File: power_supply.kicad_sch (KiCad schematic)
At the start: 18 parts, among them J2 Conn_01x01_Male, J4 Conn_01x01_Male, U4 AP63203WU, U5 AP63205WU

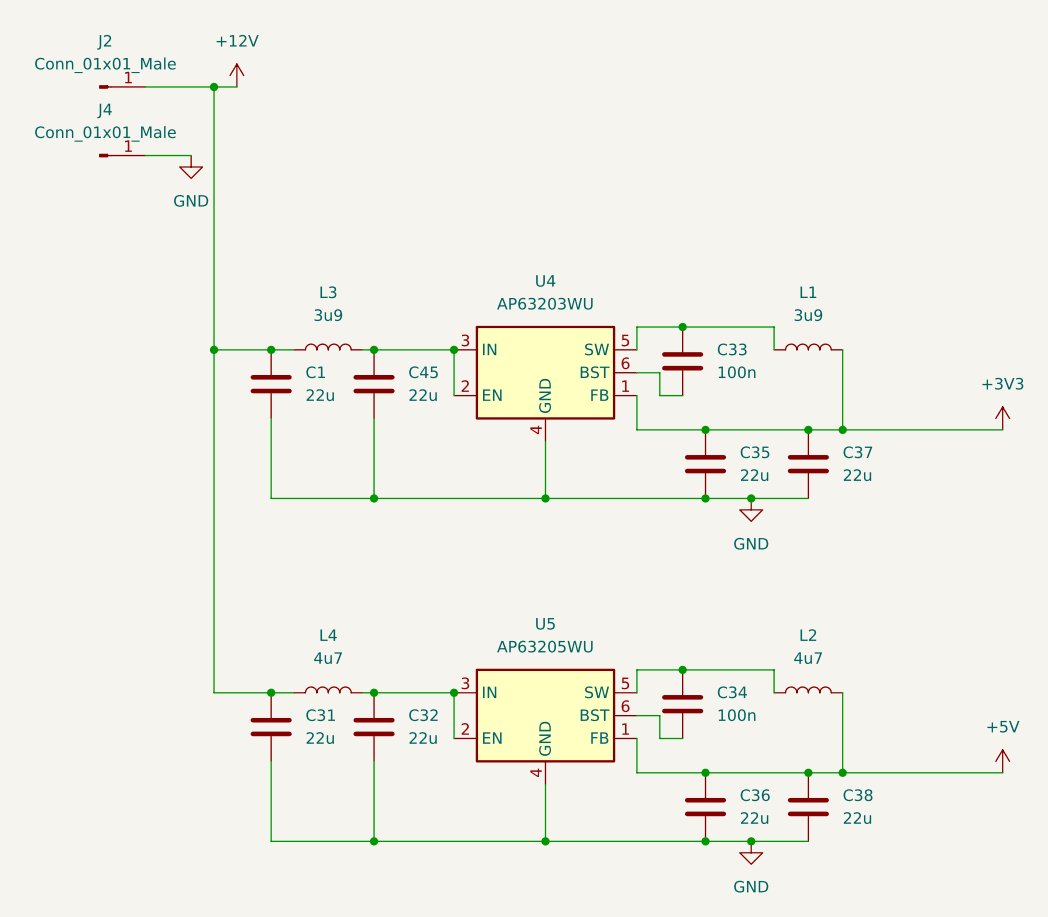
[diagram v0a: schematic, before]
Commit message: solved power drc problems
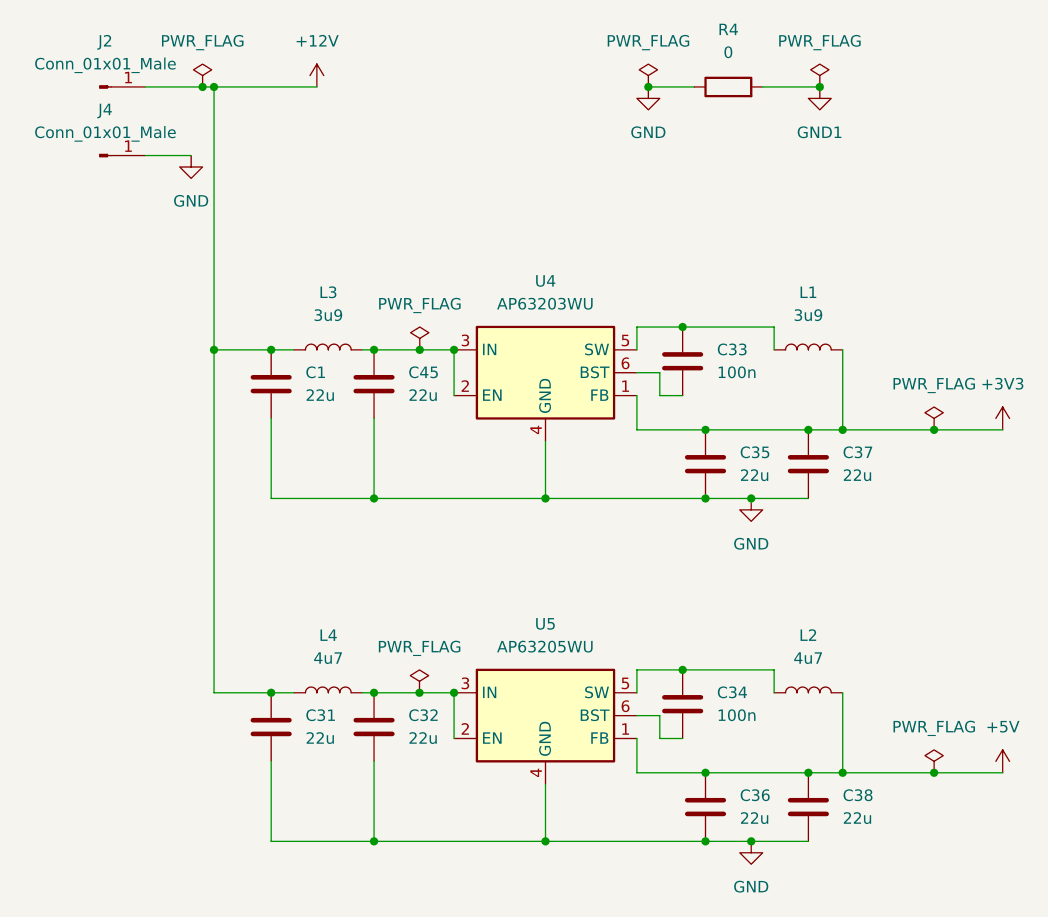
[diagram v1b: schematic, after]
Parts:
- added R4: 0, Resistor_SMD:R_0805_2012Metric_Pad1.20x1.40mm_HandSolder, symbol Device:R
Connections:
- net GND: now also R4.1
- new net GND1: R4.2

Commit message: Add SMA connector footprint and assign source
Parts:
- C1, C31, C32, C45: Source L3 store -> https://onecall.farnell.com/avx/0805zd226mat2a/cap-22-f-10v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
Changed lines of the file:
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@@
       (effects (font (size 1.27 1.27)) hide)
     )
-    (property "Source" "L3 store" (id 4) (at 120.65 67.31 0)
+    (property "Source" "https://onecall.farnell.com/avx/0805zd226mat2a/cap-22-f-10v-20-x5r-0805/dp/1867956" (id 4) (at 120.65 67.31 0)
       (effects (font (size 1.27 1.27)) hide)
     )
@@
       (effects (font (size 1.27 1.27)) hide)
     )
-    (property "Source" "L3 store" (id 4) (at 120.65 105.41 0)
+    (property "Source" "https://onecall.farnell.com/avx/0805zd226mat2a/cap-22-f-10v-20-x5r-0805/dp/1867956" (id 4) (at 120.65 105.41 0)
       (effects (font (size 1.27 1.27)) hide)
     )
@@
       (effects (font (size 1.27 1.27)) hide)
     )
-    (property "Source" "L3 store" (id 4) (at 109.22 105.41 0)
+    (property "Source" "https://onecall.farnell.com/avx/0805zd226mat2a/cap-22-f-10v-20-x5r-0805/dp/1867956" (id 4) (at 109.22 105.41 0)
       (effects (font (size 1.27 1.27)) hide)
     )
@@
       (effects (font (size 1.27 1.27)) hide)
     )
-    (property "Source" "L3 store" (id 4) (at 109.22 67.31 0)
-      (effects (font (size 1.27 1.27)) hide)
-    )
+    (property "Source" "https://onecall.farnell.com/avx/0805zd226mat2a/cap-22-f-10v-20-x5r-0805/dp/1867956" (id 4) (at 109.22 67.31 0)
+      (effects (font (size 1.27 1.27)) hide)
+    )

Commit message: added inductor to source (no footprint yet)
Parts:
- L1, L3: Source (none) -> https://onecall.farnell.com/wurth-elektronik/7440520039/ind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
- L2, L4: Source (none) -> https://www.we-online.com/components/products/datasheet/744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
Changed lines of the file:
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@@
       (effects (font (size 1.27 1.27)) hide)
     )
-    (property "Datasheet" "~" (id 3) (at 115.57 63.5 0)
+    (property "Datasheet" "https://www.we-online.com/components/products/datasheet/7440520039.pdf" (id 3) (at 115.57 63.5 0)
+      (effects (font (size 1.27 1.27)) hide)
+    )
+    (property "Source" "https://onecall.farnell.com/wurth-elektronik/7440520039/inductor-3-9uh-30-6-1x6-1mm-power/dp/2211461?st=3.9uh" (id 4) (at 115.57 63.5 0)
       (effects (font (size 1.27 1.27)) hide)
     )
@@
       (effects (font (size 1.27 1.27)) hide)
     )
-    (property "Datasheet" "~" (id 3) (at 168.91 101.6 0)
+    (property "Datasheet" "https://onecall.farnell.com/wurth-elektronik/7440530047/choke-smd-4-7uh-2-4a/dp/1635861" (id 3) (at 168.91 101.6 0)
+      (effects (font (size 1.27 1.27)) hide)
+    )
+    (property "Source" "https://www.we-online.com/components/products/datasheet/7440530047.pdf" (id 4) (at 168.91 101.6 0)
       (effects (font (size 1.27 1.27)) hide)
     )
@@
       (effects (font (size 1.27 1.27)) hide)
     )
-    (property "Datasheet" "~" (id 3) (at 115.57 101.6 0)
+    (property "Datasheet" "https://onecall.farnell.com/wurth-elektronik/7440530047/choke-smd-4-7uh-2-4a/dp/1635861" (id 3) (at 115.57 101.6 0)
+      (effects (font (size 1.27 1.27)) hide)
+    )
+    (property "Source" "https://www.we-online.com/components/products/datasheet/7440530047.pdf" (id 4) (at 115.57 101.6 0)
       (effects (font (size 1.27 1.27)) hide)
     )
@@
       (effects (font (size 1.27 1.27)) hide)
     )
-    (property "Datasheet" "~" (id 3) (at 168.91 63.5 0)
-      (effects (font (size 1.27 1.27)) hide)
-    )
+    (property "Datasheet" "https://www.we-online.com/components/products/datasheet/7440520039.pdf" (id 3) (at 168.91 63.5 0)
+      (effects (font (size 1.27 1.27)) hide)
+    )
+    (property "Source" "https://onecall.farnell.com/wurth-elektronik/7440520039/inductor-3-9uh-30-6-1x6-1mm-power/dp/2211461?st=3.9uh" (id 4) (at 168.91 63.5 0)
+      (effects (font (size 1.27 1.27)) hide)
+    )

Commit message: Add inductor footprints
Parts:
- L1, L3: footprint (none) -> Inductors:SBCP-47HY3R9B; Source https://onecall.farnell.com/wurth-elektronik/7440520039/ind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 -> https://onecall.farnell.com/kemet/sbcp-47hy3r9b/inductor-3-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
- L2, L4: footprint (none) -> Inductors:SBCP-47HY4R7B; Source https://www.we-online.com/components/products/datasheet/744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 -> https://onecall.farnell.com/kemet/sbcp-47hy4r7b/inductor-4-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
- U4: Source (none) -> https://onecall.farnell.com/diodes-inc/ap63203wu-7/dc-dc-co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
- U5: Source (none) -> https://onecall.farnell.com/diodes-inc/ap63205wu-7/dc-dc-co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
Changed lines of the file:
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@@
     (property "Reference" "L3" (id 0) (at 115.57 57.15 90))
     (property "Value" "3u9" (id 1) (at 115.57 59.69 90))
-    (property "Footprint" "" (id 2) (at 115.57 63.5 0)
-      (effects (font (size 1.27 1.27)) hide)
-    )
-    (property "Datasheet" "https://www.we-online.com/components/products/datasheet/7440520039.pdf" (id 3) (at 115.57 63.5 0)
-      (effects (font (size 1.27 1.27)) hide)
-    )
-    (property "Source" "https://onecall.farnell.com/wurth-elektronik/7440520039/inductor-3-9uh-30-6-1x6-1mm-power/dp/2211461?st=3.9uh" (id 4) (at 115.57 63.5 0)
+    (property "Footprint" "Inductors:SBCP-47HY3R9B" (id 2) (at 115.57 63.5 0)
+      (effects (font (size 1.27 1.27)) hide)
+    )
+    (property "Datasheet" "https://connect.kemet.com:7667/gateway/IntelliData-ComponentDocumentation/1.0/download/specsheet/SBCP-47HY3R9B" (id 3) (at 115.57 63.5 0)
+      (effects (font (size 1.27 1.27)) hide)
+    )
+    (property "Source" "https://onecall.farnell.com/kemet/sbcp-47hy3r9b/inductor-3-9uh-20-2-15a-radial/dp/3011792" (id 4) (at 115.57 63.5 0)
       (effects (font (size 1.27 1.27)) hide)
     )
@@
     )
     (property "Datasheet" "https://www.diodes.com/assets/Datasheets/AP63200-AP63201-AP63203-AP63205.pdf" (id 3) (at 139.7 104.14 0)
+      (effects (font (size 1.27 1.27)) hide)
+    )
+    (property "Source" "https://onecall.farnell.com/diodes-inc/ap63205wu-7/dc-dc-conv-sync-buck-1-1mhz-85deg/dp/3518308?st=ap63205" (id 4) (at 139.7 104.14 0)
       (effects (font (size 1.27 1.27)) hide)
     )
@@
     (property "Reference" "L2" (id 0) (at 168.91 95.25 90))
     (property "Value" "4u7" (id 1) (at 168.91 97.79 90))
-    (property "Footprint" "" (id 2) (at 168.91 101.6 0)
-      (effects (font (size 1.27 1.27)) hide)
-    )
-    (property "Datasheet" "https://onecall.farnell.com/wurth-elektronik/7440530047/choke-smd-4-7uh-2-4a/dp/1635861" (id 3) (at 168.91 101.6 0)
-      (effects (font (size 1.27 1.27)) hide)
-    )
-    (property "Source" "https://www.we-online.com/components/products/datasheet/7440530047.pdf" (id 4) (at 168.91 101.6 0)
+    (property "Footprint" "Inductors:SBCP-47HY4R7B" (id 2) (at 168.91 101.6 0)
+      (effects (font (size 1.27 1.27)) hide)
+    )
+    (property "Datasheet" "https://connect.kemet.com:7667/gateway/IntelliData-ComponentDocumentation/1.0/download/specsheet/SBCP-47HY4R7B" (id 3) (at 168.91 101.6 0)
+      (effects (font (size 1.27 1.27)) hide)
+    )
+    (property "Source" "https://onecall.farnell.com/kemet/sbcp-47hy4r7b/inductor-4-7uh-20-2-1a-radial/dp/3011796" (id 4) (at 168.91 101.6 0)
       (effects (font (size 1.27 1.27)) hide)
     )
@@
     (property "Reference" "L4" (id 0) (at 115.57 95.25 90))
     (property "Value" "4u7" (id 1) (at 115.57 97.79 90))
-    (property "Footprint" "" (id 2) (at 115.57 101.6 0)
-      (effects (font (size 1.27 1.27)) hide)
-    )
-    (property "Datasheet" "https://onecall.farnell.com/wurth-elektronik/7440530047/choke-smd-4-7uh-2-4a/dp/1635861" (id 3) (at 115.57 101.6 0)
-      (effects (font (size 1.27 1.27)) hide)
-    )
-    (property "Source" "https://www.we-online.com/components/products/datasheet/7440530047.pdf" (id 4) (at 115.57 101.6 0)
+    (property "Footprint" "Inductors:SBCP-47HY4R7B" (id 2) (at 115.57 101.6 0)
+      (effects (font (size 1.27 1.27)) hide)
+    )
+    (property "Datasheet" "https://connect.kemet.com:7667/gateway/IntelliData-ComponentDocumentation/1.0/download/specsheet/SBCP-47HY4R7B" (id 3) (at 115.57 101.6 0)
+      (effects (font (size 1.27 1.27)) hide)
+    )
+    (property "Source" "https://onecall.farnell.com/kemet/sbcp-47hy4r7b/inductor-4-7uh-20-2-1a-radial/dp/3011796" (id 4) (at 115.57 101.6 0)
       (effects (font (size 1.27 1.27)) hide)
     )
@@
     )
     (property "Datasheet" "https://www.diodes.com/assets/Datasheets/AP63200-AP63201-AP63203-AP63205.pdf" (id 3) (at 139.7 66.04 0)
+      (effects (font (size 1.27 1.27)) hide)
+    )
+    (property "Source" "https://onecall.farnell.com/diodes-inc/ap63203wu-7/dc-dc-conv-sync-buck-1-1mhz-85deg/dp/3518307?ost=ap63203" (id 4) (at 139.7 66.04 0)
       (effects (font (size 1.27 1.27)) hide)
     )
@@
     (property "Reference" "L1" (id 0) (at 168.91 57.15 90))
     (property "Value" "3u9" (id 1) (at 168.91 59.69 90))
-    (property "Footprint" "" (id 2) (at 168.91 63.5 0)
-      (effects (font (size 1.27 1.27)) hide)
-    )
-    (property "Datasheet" "https://www.we-online.com/components/products/datasheet/7440520039.pdf" (id 3) (at 168.91 63.5 0)
-      (effects (font (size 1.27 1.27)) hide)
-    )
-    (property "Source" "https://onecall.farnell.com/wurth-elektronik/7440520039/inductor-3-9uh-30-6-1x6-1mm-power/dp/2211461?st=3.9uh" (id 4) (at 168.91 63.5 0)
-      (effects (font (size 1.27 1.27)) hide)
-    )
+    (property "Footprint" "Inductors:SBCP-47HY3R9B" (id 2) (at 168.91 63.5 0)
+      (effects (font (size 1.27 1.27)) hide)
+    )
+    (property "Datasheet" "https://connect.kemet.com:7667/gateway/IntelliData-ComponentDocumentation/1.0/download/specsheet/SBCP-47HY3R9B" (id 3) (at 168.91 63.5 0)
+      (effects (font (size 1.27 1.27)) hide)
+    )
+    (property "Source" "https://onecall.farnell.com/kemet/sbcp-47hy3r9b/inductor-3-9uh-20-2-15a-radial/dp/3011792" (id 4) (at 168.91 63.5 0)
+      (effects (font (size 1.27 1.27)) hide)
+    )

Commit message: positioned power components
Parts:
- removed R4: 0, Resistor_SMD:R_0805_2012Metric_Pad1.20x1.40mm_HandSolder, symbol Device:R
- added JP5: SolderJumper_2_Bridged, Jumper:SolderJumper-2_P1.3mm_Bridged_Pad1.0x1.5mm, symbol Jumper:SolderJumper_2_Bridged
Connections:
- net GND: now also JP5.1 (A)
- net GND1: now also JP5.2 (B)
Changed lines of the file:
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@@
     (pin "1")
-  )
-  (symbol (lib_id "Device:R") (at 160.02 34.29 90) (unit 1)
-    (in_bom yes) (on_board yes) (fields_autoplaced)
-    (property "Reference" "R4" (id 0) (at 160.02 27.94 90))
-    (property "Value" "0" (id 1) (at 160.02 30.48 90))
-    (property "Footprint" "Resistor_SMD:R_0805_2012Metric_Pad1.20x1.40mm_HandSolder" (id 2) (at 160.02 36.068 90)
-      (effects (font (size 1.27 1.27)) hide)
-    )
-    (property "Datasheet" "~" (id 3) (at 160.02 34.29 0)
-      (effects (font (size 1.27 1.27)) hide)
-    )
-    (property "Source" "wire" (id 4) (at 160.02 34.29 0)
-      (effects (font (size 1.27 1.27)) hide)
-    )
-    (pin "1")
-    (pin "2")
   )
   (symbol (lib_id "Device:C") (at 154.94 102.87 0) (unit 1)
@@
       (effects (font (size 1.27 1.27)) hide)
     )
+    (pin "1")
+    (pin "2")
+  )
+  (symbol (lib_id "Jumper:SolderJumper_2_Bridged") (at 160.02 34.29 0) (unit 1)
+    (in_bom yes) (on_board yes) (fields_autoplaced)
+    (property "Reference" "JP5" (id 0) (at 160.02 27.94 0))
+    (property "Value" "SolderJumper_2_Bridged" (id 1) (at 160.02 30.48 0))
+    (property "Footprint" "Jumper:SolderJumper-2_P1.3mm_Bridged_Pad1.0x1.5mm" (id 2) (at 160.02 34.29 0)
+      (effects (font (size 1.27 1.27)) hide)
+    )
+    (property "Datasheet" "~" (id 3) (at 160.02 34.29 0)
+      (effects (font (size 1.27 1.27)) hide)
+    )
